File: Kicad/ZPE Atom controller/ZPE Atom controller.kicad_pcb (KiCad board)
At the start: 2 copper layers, 17 parts, among them IC1 TC4424AVPA, P1 CONN_01X18, P2 CONN_01X18, Q1 PN2222A, T1 Transformer_SP_1S, U1 SSD1306, U2 LM7805_TO220

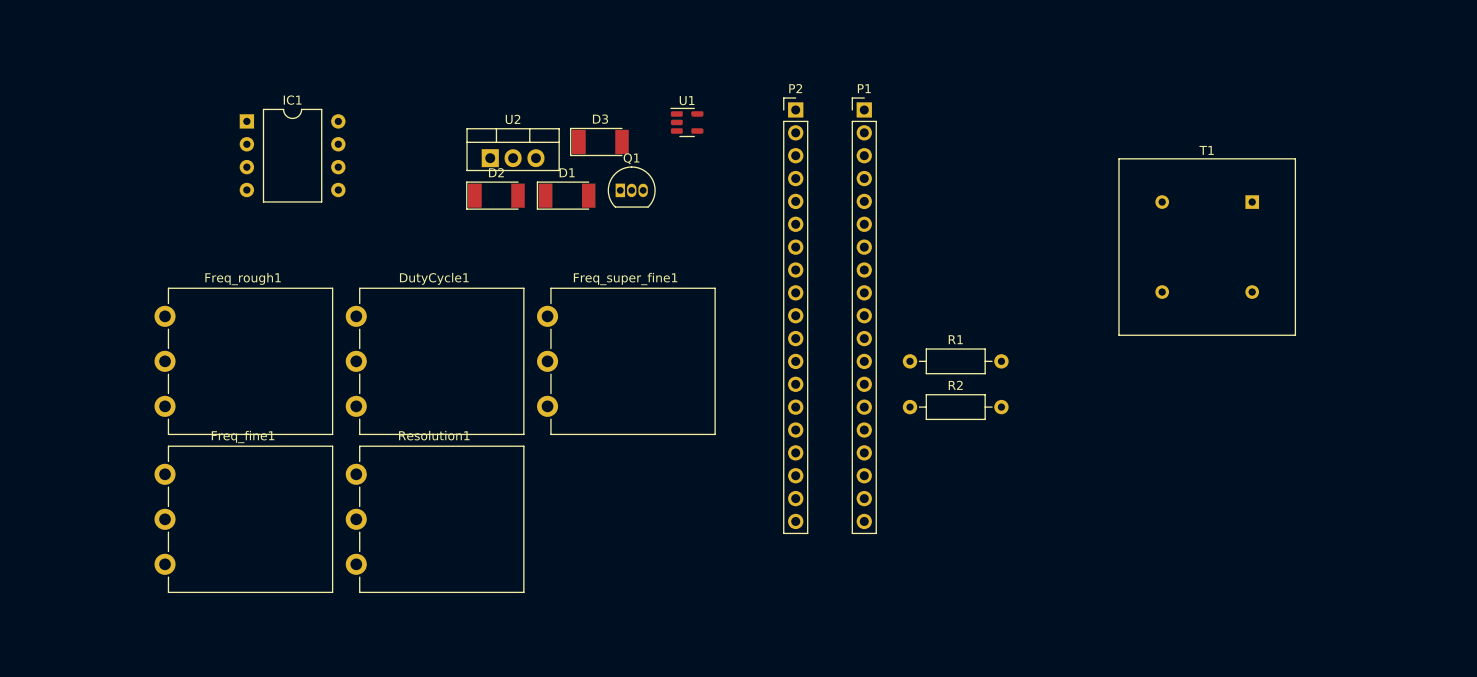
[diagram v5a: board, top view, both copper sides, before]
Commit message: added shocl 33ouH
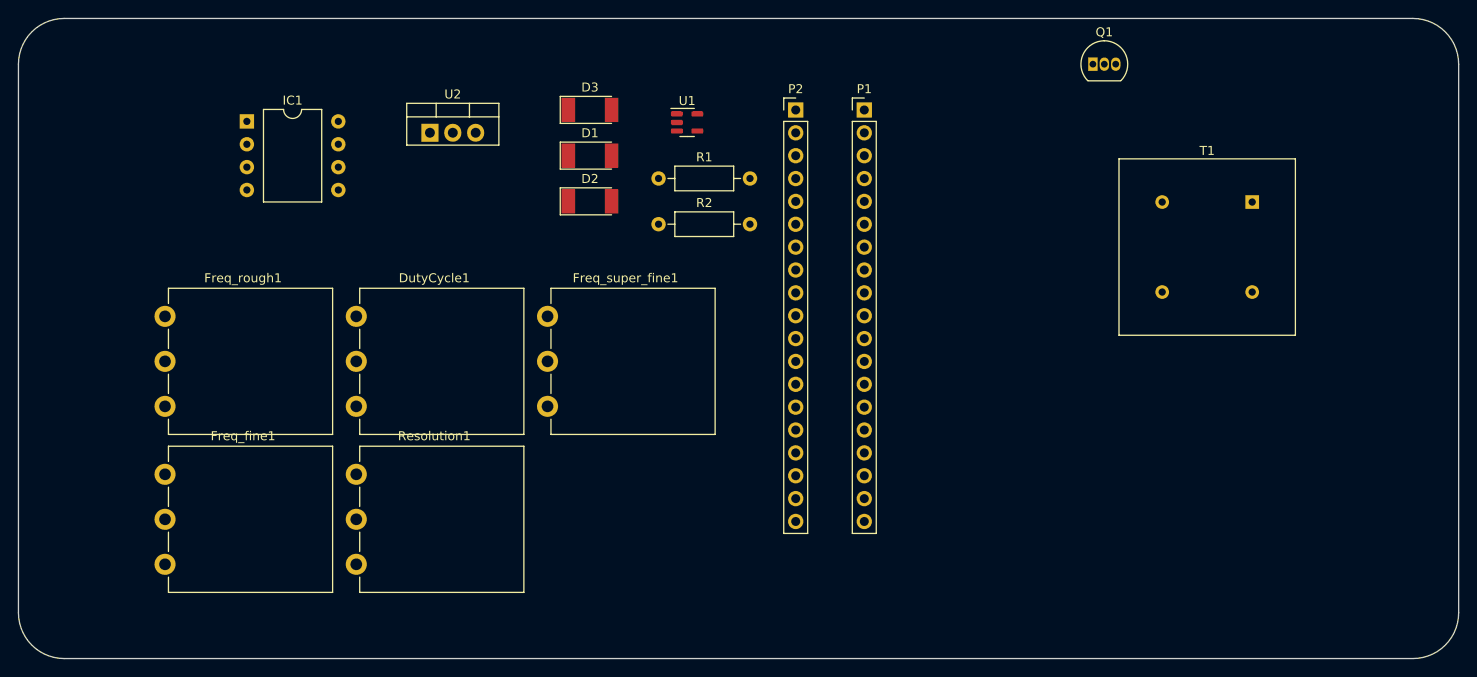
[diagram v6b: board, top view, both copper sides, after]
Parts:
- moved Q1 54.4 mm to (188.0, 66.0)
- moved R1 34.5 mm to (139.7, 78.7)
- moved R2 34.5 mm to (139.7, 83.8)
- moved D2 10.4 mm to (132.1, 81.3)
- moved U2 7.27 mm to (114.3, 73.7)
- moved D1 5.12 mm to (132.1, 76.2)
- moved D3 3.75 mm to (132.1, 71.1)
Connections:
- D1 pad 1: +12V -> Net-(D1-K)
- T1 pad 1: +12V -> Net-(D1-K)
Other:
- board outline added: 160 x 71.1 mm
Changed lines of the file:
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@@
   (net 50 "unconnected-(IC1-NC)")
   (net 51 "Net-(Q2-G)")
+  (net 52 "Net-(D1-K)")
   (footprint "Connector_PinHeader_2.54mm:PinHeader_1x19_P2.54mm_Vertical" (layer "F.Cu")
     (at 154.94 71.13)
@@
   )
   (footprint "Diode_SMD:D_MELF" (layer "F.Cu")
-    (at 133.24 74.685)
+    (at 132.08 71.12)
     (descr "Diode, MELF,,")
     (tags "Diode MELF ")
@@
   )
   (footprint "Diode_SMD:D_MELF" (layer "F.Cu")
-    (at 121.69 80.645)
+    (at 132.08 81.28)
     (descr "Diode, MELF,,")
     (tags "Diode MELF ")
@@
       (stroke (width 0.1) (type solid)) (layer "F.Fab"))
     (pad "1" thru_hole rect (at 0 0) (size 1.52 1.52) (drill 0.81) (layers *.Cu *.Mask)
-      (net 1 "+12V") (pinfunction "PR1") (pintype "passive"))
+      (net 52 "Net-(D1-K)") (pinfunction "PR1") (pintype "passive"))
     (pad "3" thru_hole circle (at 0 10) (size 1.52 1.52) (drill 0.81) (layers *.Cu *.Mask)
       (net 2 "Net-(D1-A)") (pinfunction "PR2") (pintype "passive"))
@@
   )
   (footprint "Package_TO_SOT_THT:TO-220-3_Vertical" (layer "F.Cu")
-    (at 121 76.485)
+    (at 114.3 73.66)
     (descr "TO-220-3, Vertical, RM 2.54mm, see https://www.vishay.com/docs/66542/to-220-1.pdf")
     (tags "TO-220-3 Vertical RM 2.54mm")
@@
   )
   (footprint "Diode_SMD:D_MELF" (layer "F.Cu")
-    (at 129.54 80.645)
+    (at 132.08 76.2)
     (descr "Diode, MELF,,")
     (tags "Diode MELF ")
@@
       (stroke (width 0.1) (type solid)) (layer "F.Fab"))
     (pad "1" smd rect (at -2.4 0) (size 1.5 2.7) (layers "F.Cu" "F.Paste" "F.Mask")
-      (net 1 "+12V") (pinfunction "K") (pintype "passive"))
+      (net 52 "Net-(D1-K)") (pinfunction "K") (pintype "passive"))
     (pad "2" smd rect (at 2.4 0) (size 1.5 2.7) (layers "F.Cu" "F.Paste" "F.Mask")
       (net 2 "Net-(D1-A)") (pinfunction "A") (pintype "passive"))
@@
   )
   (footprint "Package_TO_SOT_THT:TO-92_Inline" (layer "F.Cu")
-    (at 135.45 80.065)
+    (at 187.96 66.04)
     (descr "TO-92 leads in-line, narrow, oval pads, drill 0.75mm (see NXP sot054_po.pdf)")
     (tags "to-92 sc-43 sc-43a sot54 PA33 transistor")
@@
   )
   (footprint "Resistor_THT:R_Axial_DIN0207_L6.3mm_D2.5mm_P10.16mm_Horizontal" (layer "F.Cu")
-    (at 167.64 99.06)
+    (at 139.7 78.74)
     (descr "Resistor, Axial_DIN0207 series, Axial, Horizontal, pin pitch=10.16mm, 0.25W = 1/4W, length*diameter=6.3*2.5mm^2, http://cdn-reichelt.de/documents/datenblatt/B400/1_4W%23YAG.pdf")
     (tags "Resistor Axial_DIN0207 series Axial Horizontal pin pitch 10.16mm 0.25W = 1/4W length 6.3mm diameter 2.5mm")
@@
   )
   (footprint "Resistor_THT:R_Axial_DIN0207_L6.3mm_D2.5mm_P10.16mm_Horizontal" (layer "F.Cu")
-    (at 167.64 104.14)
+    (at 139.7 83.82)
     (descr "Resistor, Axial_DIN0207 series, Axial, Horizontal, pin pitch=10.16mm, 0.25W = 1/4W, length*diameter=6.3*2.5mm^2, http://cdn-reichelt.de/documents/datenblatt/B400/1_4W%23YAG.pdf")
     (tags "Resistor Axial_DIN0207 series Axial Horizontal pin pitch 10.16mm 0.25W = 1/4W length 6.3mm diameter 2.5mm")
@@
     )
   )
+  (gr_arc (start 228.6 127) (mid 227.112102 130.592102) (end 223.52 132.08)
+    (stroke (width 0.1) (type default)) (layer "Edge.Cuts"))
+  (gr_line (start 73.66 60.96) (end 223.52 60.96)
+    (stroke (width 0.1) (type default)) (layer "Edge.Cuts"))
+  (gr_line (start 228.6 66.04) (end 228.6 127)
+    (stroke (width 0.1) (type default)) (layer "Edge.Cuts"))
+  (gr_arc (start 68.58 66.04) (mid 70.067898 62.447898) (end 73.66 60.96)
+    (stroke (width 0.1) (type default)) (layer "Edge.Cuts"))
+  (gr_arc (start 223.52 60.96) (mid 227.112102 62.447898) (end 228.6 66.04)
+    (stroke (width 0.1) (type default)) (layer "Edge.Cuts"))
+  (gr_line (start 68.58 127) (end 68.58 66.04)
+    (stroke (width 0.1) (type default)) (layer "Edge.Cuts"))
+  (gr_arc (start 73.66 132.08) (mid 70.067898 130.592102) (end 68.58 127)
+    (stroke (width 0.1) (type default)) (layer "Edge.Cuts"))
+  (gr_line (start 223.52 132.08) (end 73.66 132.08)
+    (stroke (width 0.1) (type default)) (layer "Edge.Cuts"))
 )

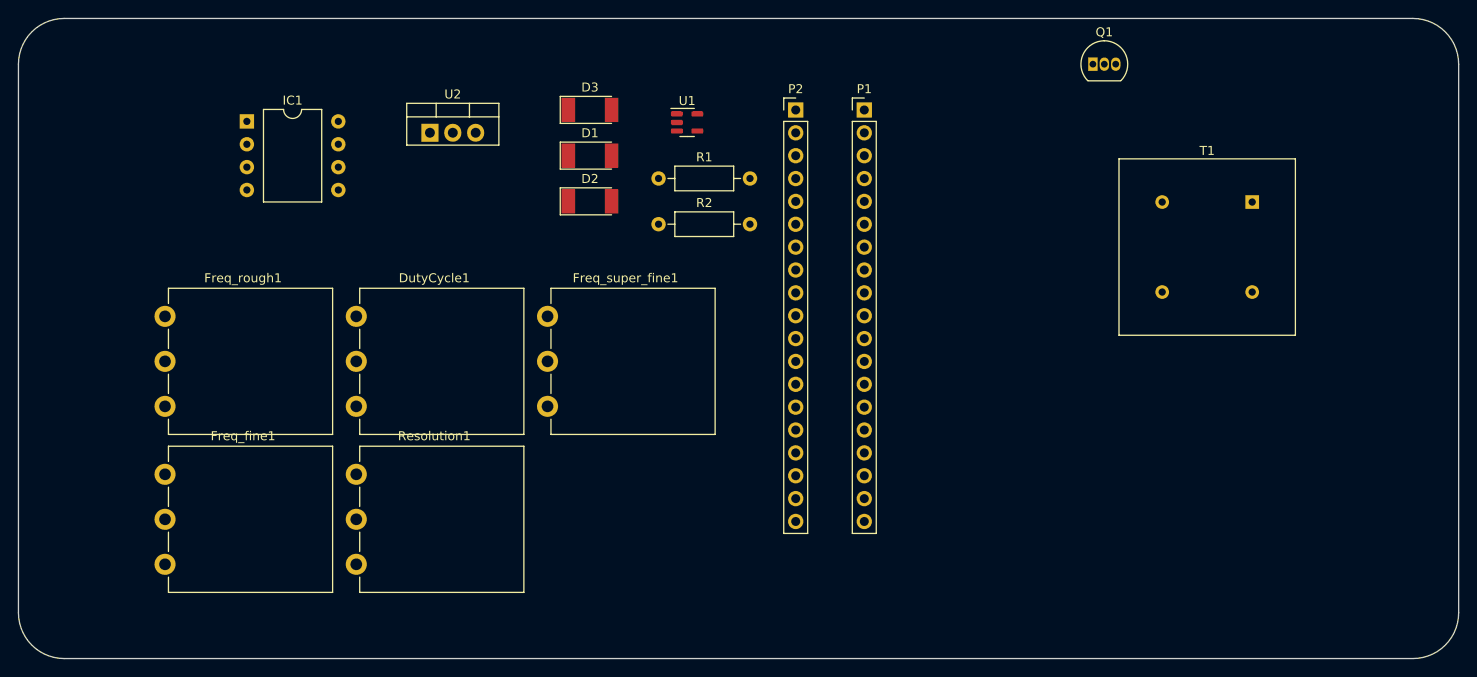
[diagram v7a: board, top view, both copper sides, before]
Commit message: Updated schematic and  code for analog input
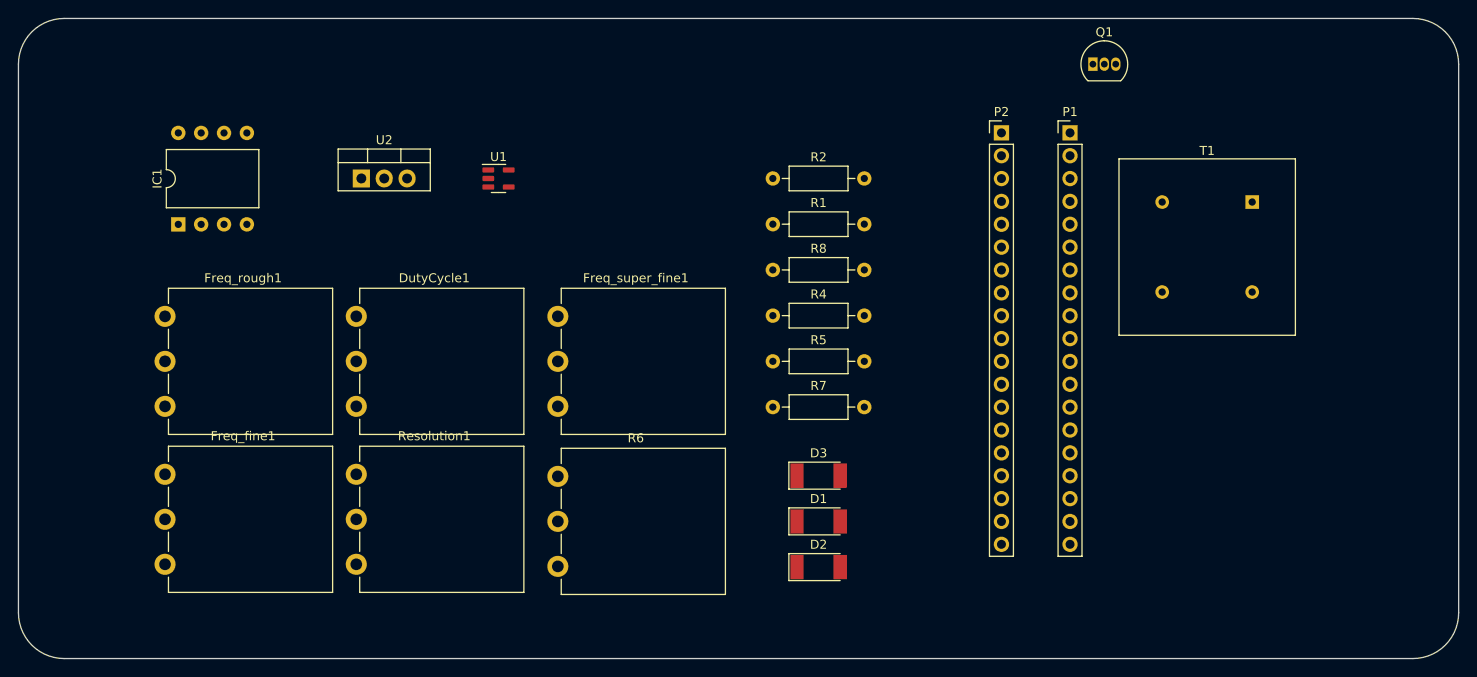
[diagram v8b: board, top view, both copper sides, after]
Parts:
- added R4: 1M, Resistor_THT:R_Axial_DIN0207_L6.3mm_D2.5mm_P10.16mm_Horizontal, F.Cu at (152.4, 94.0)
- added R5: 1k, Resistor_THT:R_Axial_DIN0207_L6.3mm_D2.5mm_P10.16mm_Horizontal, F.Cu at (152.4, 99.1)
- added R6: 100, Potentiometer_THT:Potentiometer_Piher_PC-16_Single_Vertical, F.Cu at (128.5, 121.8)
- added R7: 1M, Resistor_THT:R_Axial_DIN0207_L6.3mm_D2.5mm_P10.16mm_Horizontal, F.Cu at (152.4, 104.1)
- added R8: 1k, Resistor_THT:R_Axial_DIN0207_L6.3mm_D2.5mm_P10.16mm_Horizontal, F.Cu at (152.4, 88.9)
- moved D1 47.9 mm to (157.5, 116.8)
- moved D2 47.9 mm to (157.5, 121.9)
- moved D3 47.9 mm to (157.5, 111.8)
- moved P2 23.0 mm to (177.8, 73.7)
- moved P1 23.0 mm to (185.4, 73.7)
- moved U1 21.9 mm to (121.9, 78.7)
- moved IC1 13.7 mm to (86.3, 83.8), turned to 90 degrees
- moved R1 13.7 mm to (152.4, 83.8)
- moved R2 13.7 mm to (152.4, 78.7)
- moved U2 9.16 mm to (106.7, 78.7)
- moved Freq_super_fine1 1.14 mm to (128.5, 104.1)
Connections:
- T1 pad 3: Net-(D1-A) -> Net-(T1-SA)
- T1 pad 4: Net-(T1-S1) -> Net-(D2-K)
